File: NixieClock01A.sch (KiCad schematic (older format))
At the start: 107 parts, among them J1 Conn_01x06_Male, J10 Conn_01x01_Male, J11 Conn_01x01_Male, J12 Conn_01x01_Male, J13 Conn_01x02_Male, J14 Conn_01x04_Male, J2 Conn_02x16_Odd_Even, J3 Conn_02x16_Odd_Even, J4 USB_B_Micro, J5 Conn_01x01_Male, J6 Conn_01x01_Male, J7 Conn_01x01_Male, J8 Conn_01x01_Male, J9 Conn_01x01_Male, Q1 Q_NMOS_GDS, U1 74141, U11 74141, U12 74141, U13 74141, U2 PCF8574, U3 ESP-12E, U4 LM3478, U5 74141, U6 PCF8574, U7 PCF8574, U8 74141, U9 TC1262-33

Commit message: BJT transistors test. added Arduino Mega dimensions
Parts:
- removed C1, C11, C15, C17, C18, C19, C2, C20, C21, C22, C23, C24, C27, C28, C3, C31, C5: 100n, Capacitor_SMD:C_0603_1608Metric, symbol Device:C
- removed C16, C4: TPSC107K010R0075, Capacitor_Tantalum_SMD:CP_EIA-6032-28_Kemet-C, symbol Device:CP
- removed C26: 10u, Capacitor_SMD:C_0805_2012Metric, symbol Device:C
- removed C30: 1u, Capacitor_SMD:C_0603_1608Metric, symbol Device:C
- removed D2, D3, D4, D5, D6, D7: WS2812B, LED_SMD:LED_WS2812B_PLCC4_5.0x5.0mm_P3.2mm, symbol LED:WS2812B
- removed D8: D_TVS, Diode_SMD:D_SMC, symbol Device:D_TVS
- removed F1: Fuse, Fuse:Fuse_1206_3216Metric, symbol Device:Fuse
- removed J1: Conn_01x06_Male, Connector_PinHeader_2.54mm:PinHeader_1x06_P2.54mm_Vertical, symbol Connector:Conn_01x06_Male
- removed J13: Conn_01x02_Male, Connector_PinHeader_2.54mm:PinHeader_1x02_P2.54mm_Vertical, symbol Connector:Conn_01x02_Male
- removed J14: Conn_01x04_Male, Connector_PinSocket_2.54mm:PinSocket_1x04_P2.54mm_Vertical, symbol Connector:Conn_01x04_Male
- removed J2, J3: Conn_02x16_Odd_Even, Connector_PinSocket_2.54mm:PinSocket_2x16_P2.54mm_Vertical, symbol Connector_Generic:Conn_02x16_Odd_Even
- removed J4: USB_B_Micro, Connector_USB:USB_Micro-B_Molex-105017-0001, symbol Connector:USB_B_Micro
- removed R1, R19, R20: R, Resistor_SMD:R_0603_1608Metric, symbol Device:R
- removed R2, R3, R4, R5, R6: 12k, Resistor_SMD:R_0603_1608Metric, symbol Device:R
- removed R31, R32: 4K7, Resistor_SMD:R_0603_1608Metric, symbol Device:R
- removed R7: 330k, Resistor_SMD:R_0603_1608Metric, symbol Device:R
- removed R8: 100k, Resistor_SMD:R_0603_1608Metric, symbol Device:R
- removed R9: 470R, Resistor_SMD:R_0603_1608Metric, symbol Device:R
- removed U1, U11, U12, U5, U8: 74141, Package_DIP:DIP-16_W7.62mm, symbol 74xx_IEEE:74141
- removed U2, U6, U7: PCF8574, Package_SO:SOIC-16W_5.3x10.2mm_P1.27mm, symbol Interface_Expansion:PCF8574
- removed U3: ESP-12E, riske-lib:ESP-12E, symbol RF_Module:ESP-12E
- removed U9: TC1262-33, Package_TO_SOT_SMD:SOT-223, symbol Regulator_Linear:TC1262-33
- added Q10, Q11, Q2, Q3, Q4, Q5, Q6, Q7, Q8, Q9: Q_NPN_BEC, Package_TO_SOT_SMD:SOT-23, symbol device:Q_NPN_BEC
- added R1, R19, R2, R3, R4, R5, R6, R7, R8, R9: 100R, Resistor_SMD:R_0603_1608Metric, symbol NixieClock01A-rescue:R-Device
- C10, C12, C13, C32, C6, C7, C8, C9: symbol Device:C -> NixieClock01A-rescue:C-Device
- C14: symbol Device:CP -> NixieClock01A-rescue:CP-Device
- D1: symbol Device:D_Schottky -> NixieClock01A-rescue:D_Schottky-Device
- L1: symbol Device:L_Core_Ferrite -> NixieClock01A-rescue:L_Core_Ferrite-Device
- LA1, LA2: symbol Device:Lamp_Flash -> NixieClock01A-rescue:Lamp_Flash-Device
- N1, N2, N3, N4, N5, N6: symbol mynixies:ZM1080 -> NixieClock01A-rescue:ZM1080-mynixies
- Q1: symbol Device:Q_NMOS_GDS -> NixieClock01A-rescue:Q_NMOS_GDS-Device
- R10, R11, R12, R13, R14, R15, R16, R17, R18, R21, R22, R23, R24, R25, R26, R27, R28, R29, R30: symbol Device:R -> NixieClock01A-rescue:R-Device
- U13: symbol 74xx_IEEE:74141 -> NixieClock01A-rescue:74141-74xx_IEEE
- U4: symbol lm3478:LM3478 -> NixieClock01A-rescue:LM3478-lm3478
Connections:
- net labels removed: +3V3, A1, A2, A3, A4, ADC, ADC-IN, B1, B2, B3, B4, C1, C2, C3, C4, D1, D2, D3, D4, E1, E2, E3, E4, EN, GPIO0, GPIO15, GPIO2, NeoPix, RST, RX, SCL, SDA, TX
- wire segments 392 -> 222
- no-connect marks 27 -> 12

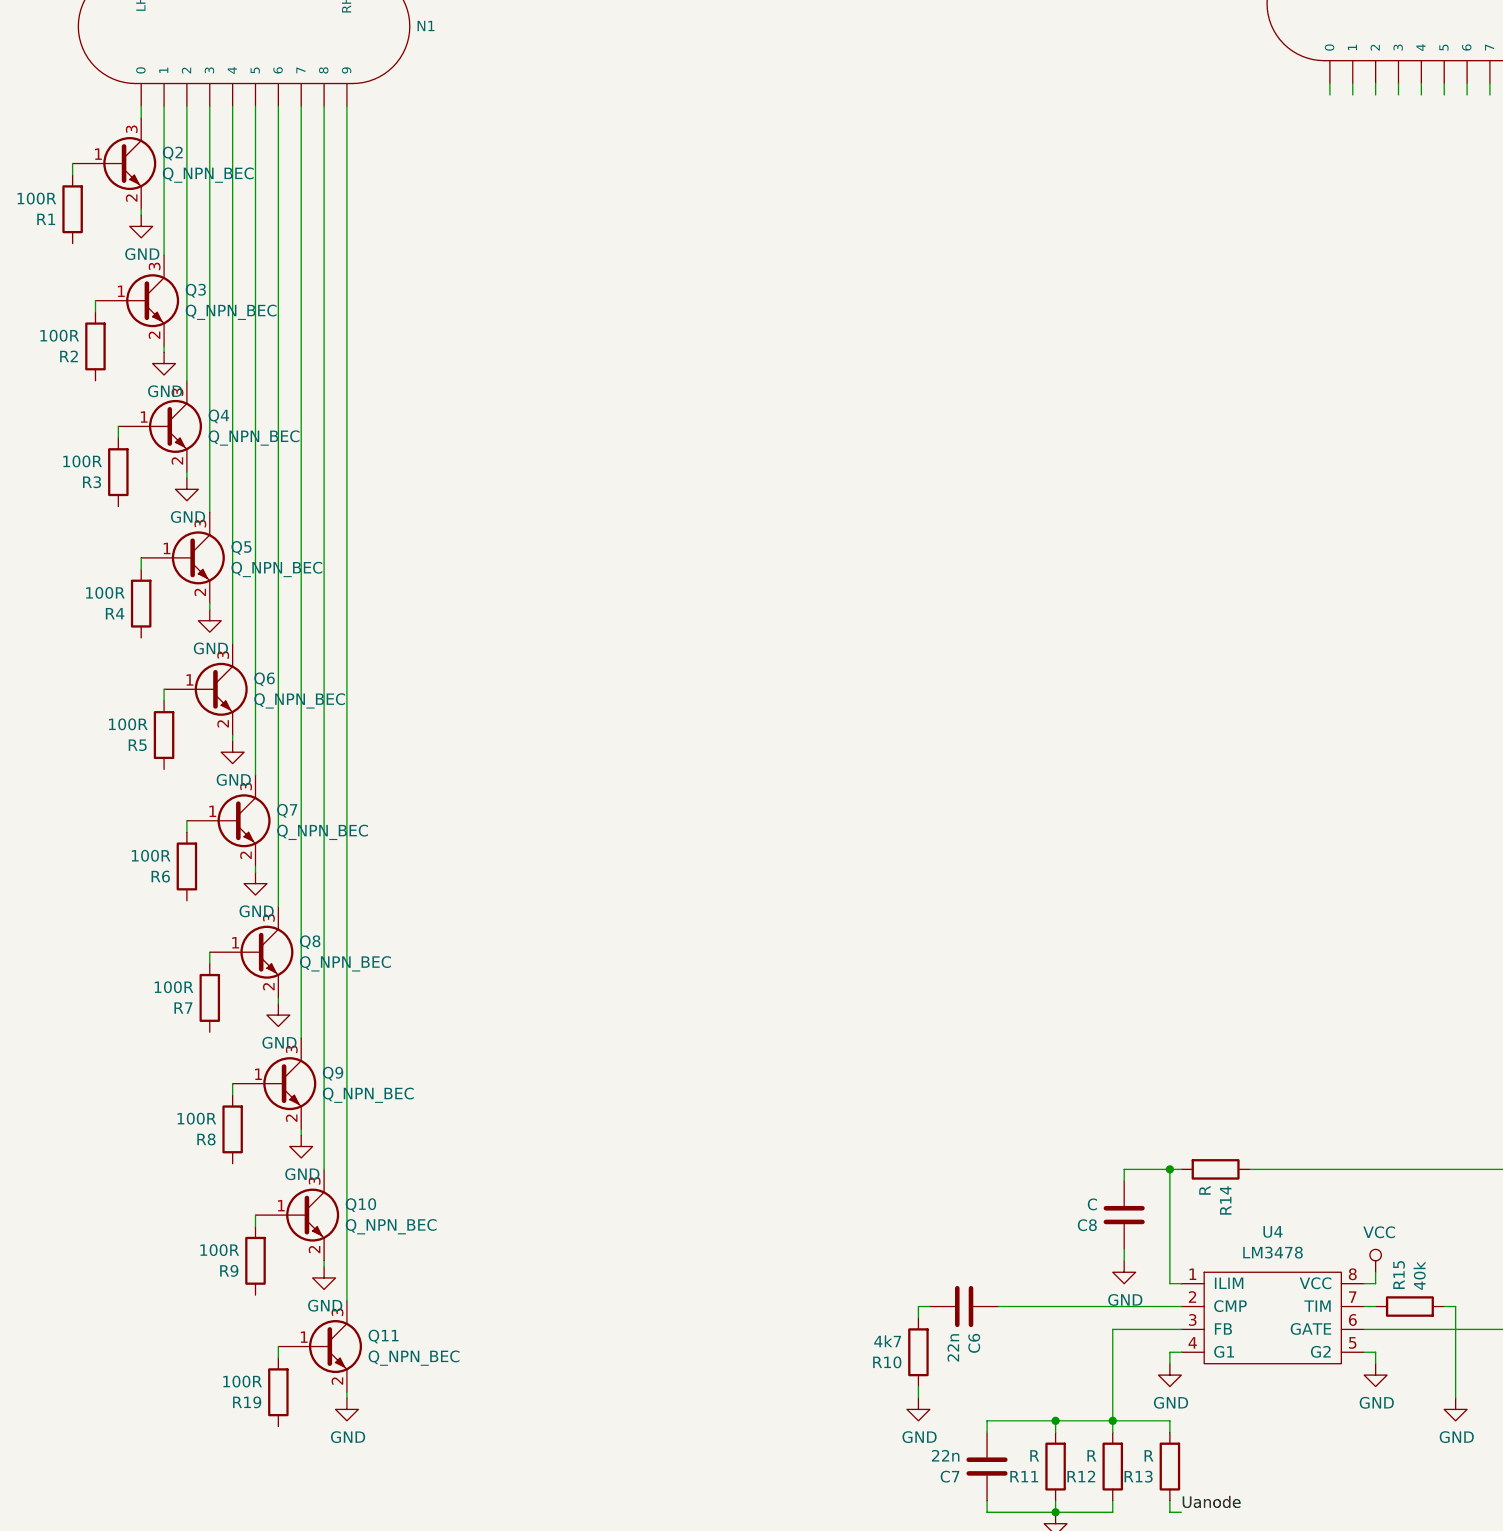
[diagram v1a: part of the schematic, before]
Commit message: Added Arduino Mega dimensions, Added DS3231
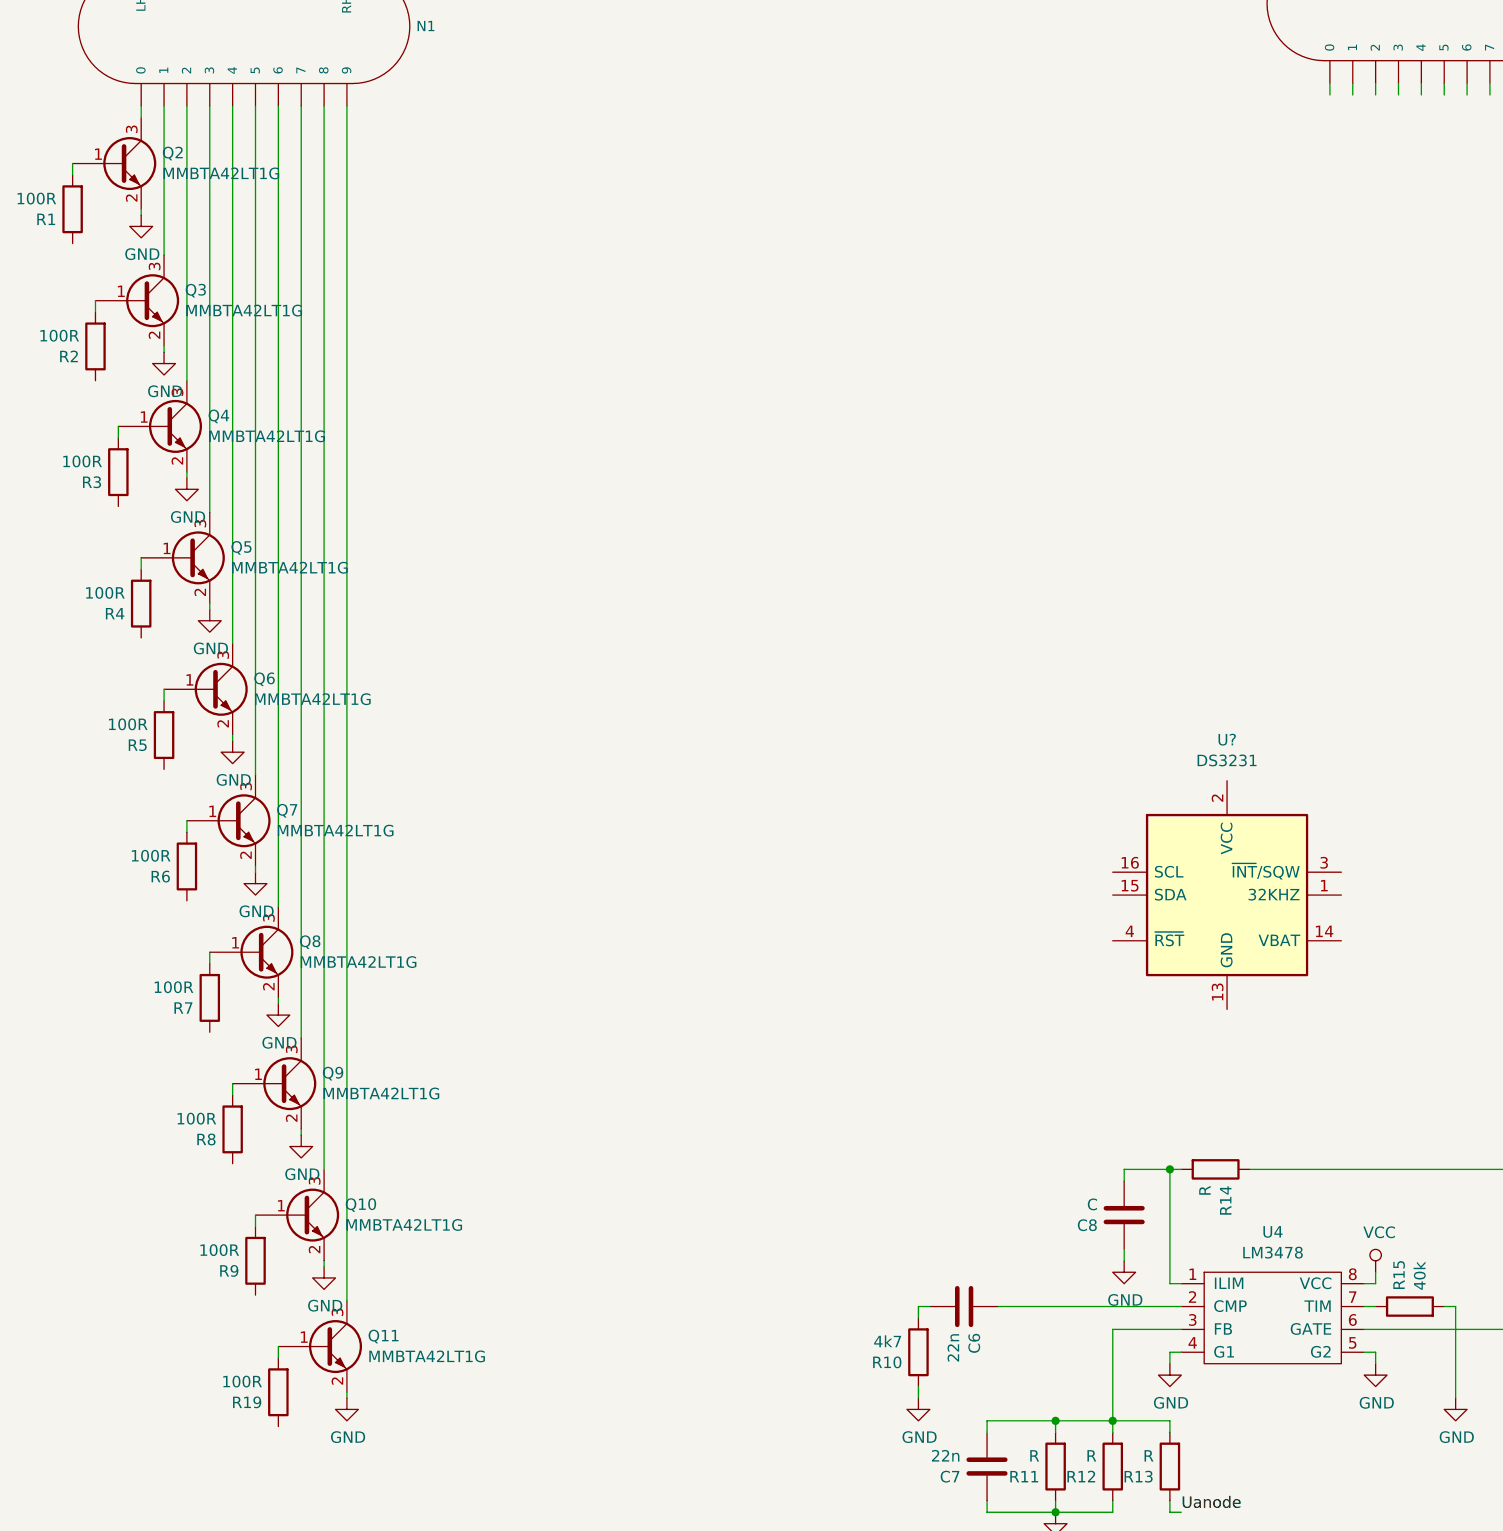
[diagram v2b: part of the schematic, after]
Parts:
- added U?: DS3231, Housings_SOIC:SOIC-16_7.5x10.3mm_Pitch1.27mm, symbol maxim:DS3231
- Q10, Q11, Q2, Q3, Q4, Q5, Q6, Q7, Q8, Q9: value Q_NPN_BEC -> MMBTA42LT1G
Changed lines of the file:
@@
 P -2650 1650
 F 0 "Q2" H -2459 1696 50  0000 L CNN
-F 1 "Q_NPN_BEC" H -2459 1605 50  0000 L CNN
+F 1 "MMBTA42LT1G" H -2459 1605 50  0000 L CNN
 F 2 "Package_TO_SOT_SMD:SOT-23" H -2450 1750 50  0001 C CNN
 F 3 "" H -2650 1650 50  0001 C CNN
@@
 P -2550 2250
 F 0 "Q3" H -2359 2296 50  0000 L CNN
-F 1 "Q_NPN_BEC" H -2359 2205 50  0000 L CNN
+F 1 "MMBTA42LT1G" H -2359 2205 50  0000 L CNN
 F 2 "Package_TO_SOT_SMD:SOT-23" H -2350 2350 50  0001 C CNN
 F 3 "" H -2550 2250 50  0001 C CNN
@@
 P -2450 2800
 F 0 "Q4" H -2259 2846 50  0000 L CNN
-F 1 "Q_NPN_BEC" H -2259 2755 50  0000 L CNN
+F 1 "MMBTA42LT1G" H -2259 2755 50  0000 L CNN
 F 2 "Package_TO_SOT_SMD:SOT-23" H -2250 2900 50  0001 C CNN
 F 3 "" H -2450 2800 50  0001 C CNN
@@
 P -2350 3375
 F 0 "Q5" H -2159 3421 50  0000 L CNN
-F 1 "Q_NPN_BEC" H -2159 3330 50  0000 L CNN
+F 1 "MMBTA42LT1G" H -2159 3330 50  0000 L CNN
 F 2 "Package_TO_SOT_SMD:SOT-23" H -2150 3475 50  0001 C CNN
 F 3 "" H -2350 3375 50  0001 C CNN
@@
 P -2250 3950
 F 0 "Q6" H -2059 3996 50  0000 L CNN
-F 1 "Q_NPN_BEC" H -2059 3905 50  0000 L CNN
+F 1 "MMBTA42LT1G" H -2059 3905 50  0000 L CNN
 F 2 "Package_TO_SOT_SMD:SOT-23" H -2050 4050 50  0001 C CNN
 F 3 "" H -2250 3950 50  0001 C CNN
@@
 P -2150 4525
 F 0 "Q7" H -1959 4571 50  0000 L CNN
-F 1 "Q_NPN_BEC" H -1959 4480 50  0000 L CNN
+F 1 "MMBTA42LT1G" H -1959 4480 50  0000 L CNN
 F 2 "Package_TO_SOT_SMD:SOT-23" H -1950 4625 50  0001 C CNN
 F 3 "" H -2150 4525 50  0001 C CNN
@@
 P -2050 5100
 F 0 "Q8" H -1859 5146 50  0000 L CNN
-F 1 "Q_NPN_BEC" H -1859 5055 50  0000 L CNN
+F 1 "MMBTA42LT1G" H -1859 5055 50  0000 L CNN
 F 2 "Package_TO_SOT_SMD:SOT-23" H -1850 5200 50  0001 C CNN
 F 3 "" H -2050 5100 50  0001 C CNN
@@
 P -1950 5675
 F 0 "Q9" H -1759 5721 50  0000 L CNN
-F 1 "Q_NPN_BEC" H -1759 5630 50  0000 L CNN
+F 1 "MMBTA42LT1G" H -1759 5630 50  0000 L CNN
 F 2 "Package_TO_SOT_SMD:SOT-23" H -1750 5775 50  0001 C CNN
 F 3 "" H -1950 5675 50  0001 C CNN
@@
 P -1850 6250
 F 0 "Q10" H -1659 6296 50  0000 L CNN
-F 1 "Q_NPN_BEC" H -1659 6205 50  0000 L CNN
+F 1 "MMBTA42LT1G" H -1659 6205 50  0000 L CNN
 F 2 "Package_TO_SOT_SMD:SOT-23" H -1650 6350 50  0001 C CNN
 F 3 "" H -1850 6250 50  0001 C CNN
@@
 P -1750 6825
 F 0 "Q11" H -1559 6871 50  0000 L CNN
-F 1 "Q_NPN_BEC" H -1559 6780 50  0000 L CNN
+F 1 "MMBTA42LT1G" H -1559 6780 50  0000 L CNN
 F 2 "Package_TO_SOT_SMD:SOT-23" H -1550 6925 50  0001 C CNN
 F 3 "" H -1750 6825 50  0001 C CNN
@@
 F1 "nixies.sch" 50
 $EndSheet
+$Comp
+L maxim:DS3231 U?
+U 1 1 5C91F40C
+P 2200 4850
+F 0 "U?" H 2200 5528 50  0000 C CNN
+F 1 "DS3231" H 2200 5437 50  0000 C CNN
+F 2 "Housings_SOIC:SOIC-16_7.5x10.3mm_Pitch1.27mm" H 2250 4450 50  0001 L CNN
+F 3 "http://datasheets.maximintegrated.com/en/ds/DS3231.pdf" H 2470 5100 50  0001 C CNN
+	1    2200 4850
+	1    0    0    -1
+$EndComp
 $EndSCHEMATC

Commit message: Added pin headers for Arduino Mega. Added first two nixies, Changed PCB dimensions
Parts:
- removed C32: 100n, Capacitor_SMD:C_0603_1608Metric, symbol NixieClock01A-rescue:C-Device
- removed J10, J11, J12, J9: Conn_01x01_Male, MountingHole:MountingHole_3.2mm_M3_DIN965_Pad, symbol Connector:Conn_01x01_Male
- removed N1, N2, N3, N4, N5, N6: ZM1080, riske-lib:ZM1080, symbol NixieClock01A-rescue:ZM1080-mynixies
- removed Q10, Q11, Q2, Q3, Q4, Q5, Q6, Q7, Q8, Q9: MMBTA42LT1G, Package_TO_SOT_SMD:SOT-23, symbol device:Q_NPN_BEC
- removed R1, R19, R2, R3, R4, R5, R6, R7, R8, R9: 100R, Resistor_SMD:R_0603_1608Metric, symbol NixieClock01A-rescue:R-Device
- removed R21, R22, R23, R24, R25, R26: 27k, Resistor_SMD:R_1206_3216Metric, symbol NixieClock01A-rescue:R-Device
- removed U13: 74141, Package_DIP:DIP-16_W7.62mm, symbol NixieClock01A-rescue:74141-74xx_IEEE
- added J1: Conn_01x10, Connector_PinSocket_2.54mm:PinSocket_1x10_P2.54mm_Vertical, symbol Connector:Conn_01x10
- added J13: Conn_02x18_Odd_Even, Connector_PinHeader_2.54mm:PinHeader_2x18_P2.54mm_Vertical, symbol Connector:Conn_02x18_Odd_Even
- added J14, J15, J2, J3, J4: Conn_01x08, Connector_PinSocket_2.54mm:PinSocket_1x08_P2.54mm_Vertical, symbol Connector:Conn_01x08
- gave numbers to parts that had none: 1
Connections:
- net labels added: +3.3V, 10, 11, 12, 13, 14, 15, 16, 17, 18, 19, 2, 20, 21, 22, 23, 24, 25, 26, 27, 28, 29, 3, 30, 31, 32, 33, 34, 35, 36, 37, 38, 39, 4, 40, 41, 42, 43, 44, 45, 46, 47, 48, 49, 5, 50, 51, 52, 53, 6, 7, 8, 9, A0, A1, A10, A11, A12, A13, A14, A15, A2, A3, A4, A5, A6, A7, A8, A9, AREF, IOREF, RES, RX, SCL, SDA, TX
- net labels removed: F1, F2, F3, F4
- wire segments 222 -> 139
- no-connect marks 12 -> 1
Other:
- note added: "Arduino Mega"
- moved on the sheet: C10, C12, C13, C14, C6, C7, C8, C9, D1, J5, J6, J7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
